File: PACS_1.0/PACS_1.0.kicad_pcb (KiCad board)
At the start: 2 copper layers, 73.6 x 42.7 mm, 47 parts, among them J1 Conn_01x04_Socket, J2 Conn_01x02_Pin, Q1 PN2222A, U1 MSP430G2553IN20, U2 S-80855CNMC-B9GT2U, U3 BSS84PH6327XTSA2, U4 TPS562201DDCR, U5 MCP9700Ax-ETT, U6 LTR-303ALS-01, U7 XB24CZ7WIT-004

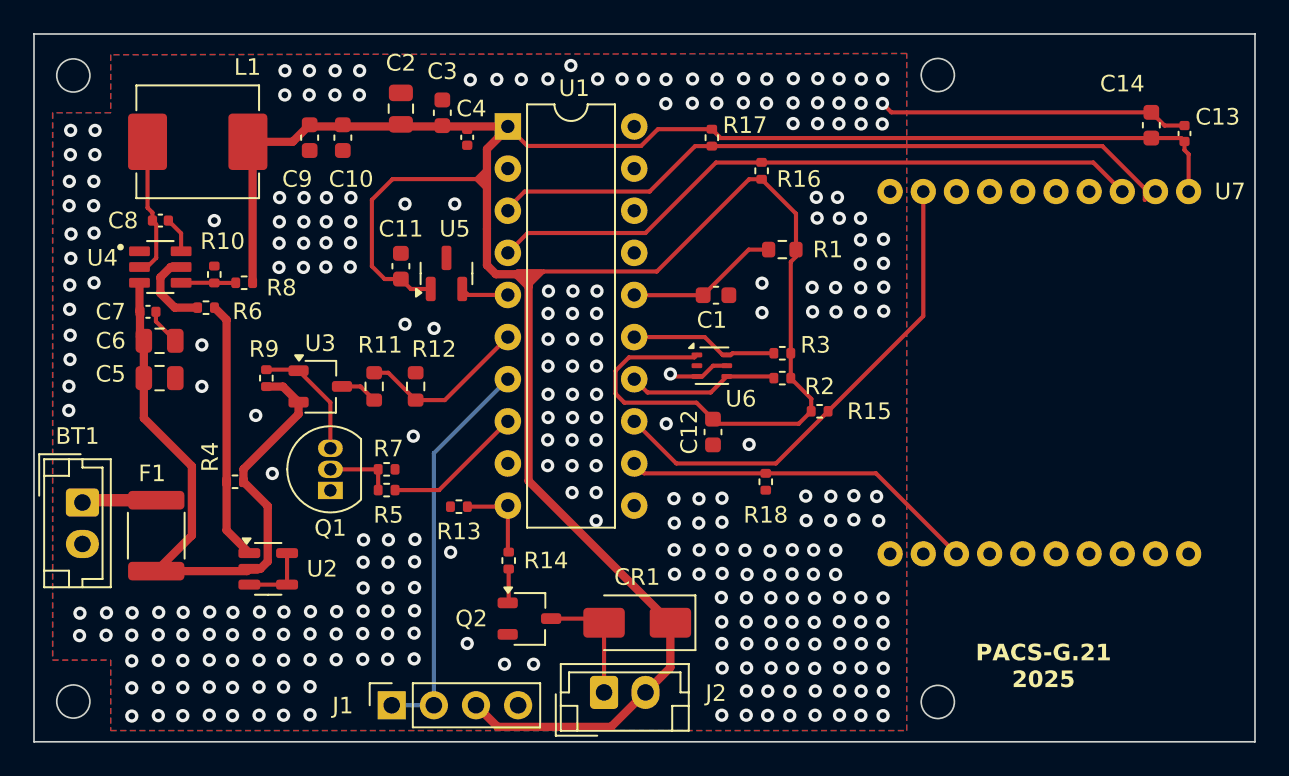
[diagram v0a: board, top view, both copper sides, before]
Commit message: revised PCB with Zoltan housekeeping
still needs tons of vias for stitching ground planes
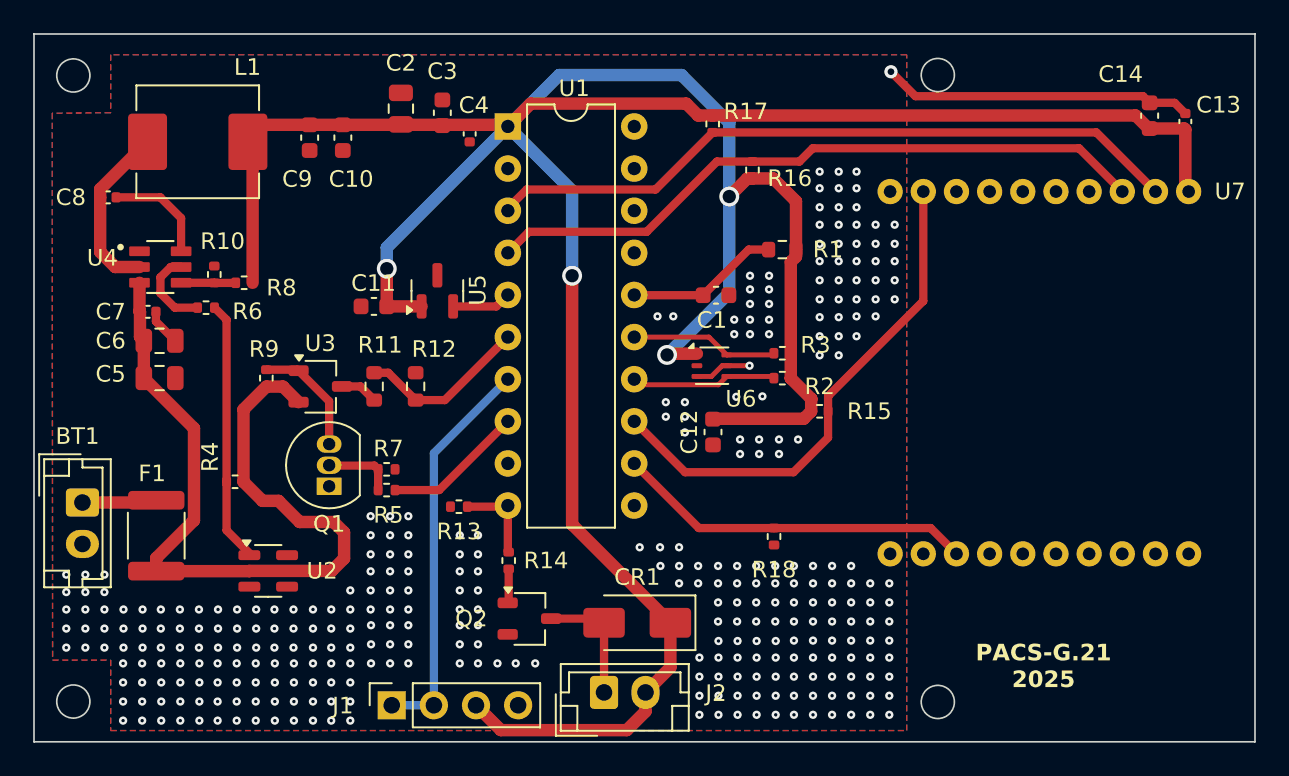
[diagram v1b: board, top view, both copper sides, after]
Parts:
- moved C8 3.45 mm to (147.6, 78.6)
- moved R18 3.34 mm to (187.8, 99.0)
- moved C11 2.92 mm to (163.6, 85.2), turned to 0 degrees
- moved U5 1.19 mm to (167.4, 84.2)
- moved R17 0.83 mm to (184.1, 74.2)
- moved C13 0.73 mm to (212.6, 74.0)
- moved C14 0.58 mm to (210.4, 73.7)
- moved R16 0.55 mm to (186.4, 77.0)
- moved Q1 0.26 mm to (160.9, 96.0)
- moved C4 0.25 mm to (169.4, 74.8)
- moved U2 0.12 mm to (157.2, 101.1)
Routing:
- net Net-(U2-VDD): track 40.5 -> 48.9 mm
- net +3.3V: track 189.4 -> 196.0 mm, vias 0 -> 4
- net GND: track 28.9 -> 24.5 mm, vias 280 -> 326
- net Net-(U4-VBST): track 2.17 -> 6.44 mm
- net Net-(U4-SW): track 8.46 -> 10.6 mm
- net /Zigbee Module/SLEEP_RQ: track 29.7 -> 31.0 mm
- net /Zigbee Module/Rx: track 40.0 -> 40.7 mm
- net /Sensors/A_Temp: track 2.90 -> 3.59 mm

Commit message: Finished stitching vias
i think officially complete
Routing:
- net GND: track 24.5 -> 27.4 mm, vias 326 -> 692
